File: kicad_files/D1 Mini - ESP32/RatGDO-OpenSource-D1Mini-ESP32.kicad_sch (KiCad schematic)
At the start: 7 parts, among them J1 Screw_Terminal_01x03, Q1 2N7002, Q2 AO3400A, U2 mini_esp32

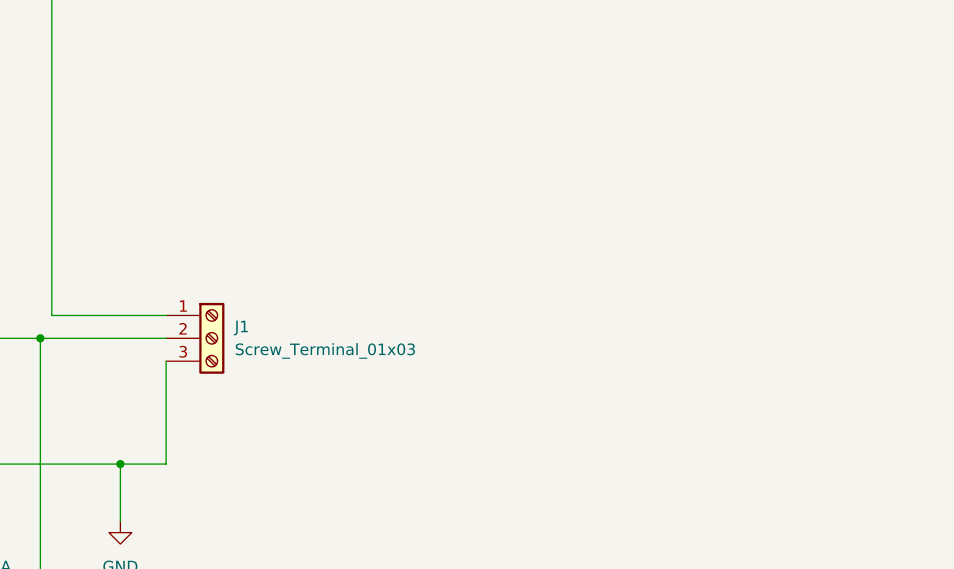
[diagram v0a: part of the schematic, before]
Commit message: Fixed Bad PCB Labeling
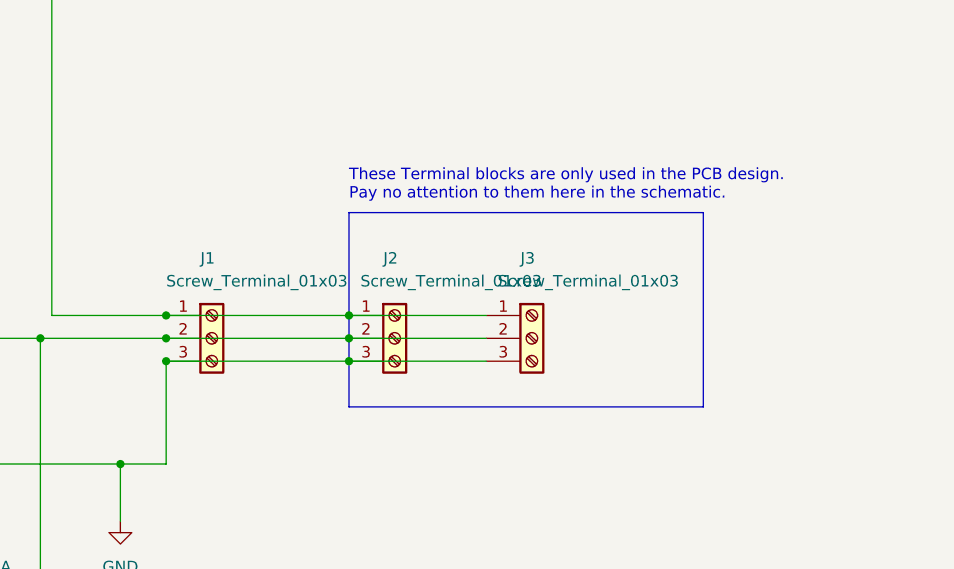
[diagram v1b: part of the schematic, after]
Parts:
- added J2: Screw_Terminal_01x03, Connector_Phoenix_MC:PhoenixContact_MCV_1,5_3-G-3.5_1x03_P3.50mm_Vertical, symbol Connector:Screw_Terminal_01x03
- added J3: Screw_Terminal_01x03, Connector_PinHeader_2.54mm:PinHeader_1x03_P2.54mm_Vertical, symbol Connector:Screw_Terminal_01x03
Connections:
- net GND: now also J2.3 (Pin_3), J3.3 (Pin_3)
- net at J1.1 (Pin_1), R1.1: now also J2.1 (Pin_1), J3.1 (Pin_1)
- net at J1.2 (Pin_2), Q1.1 (G), Q2.3 (D): now also J2.2 (Pin_2), J3.2 (Pin_2)
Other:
- note added: "These Terminal blocks are only used in the PCB design. Pay no attention to them here in the schematic."
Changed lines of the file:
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@@
 (kicad_sch (version 20230121) (generator eeschema)
   (paper "A4")
+  (junction (at 177.8 90.17) (diameter 0) (color 0 0 0 0)
+  )
   (junction (at 105.41 105.41) (diameter 0) (color 0 0 0 0)
   )
+  (junction (at 157.48 92.71) (diameter 0) (color 0 0 0 0)
+  )
   (junction (at 152.4 104.14) (diameter 0) (color 0 0 0 0)
   )
+  (junction (at 157.48 87.63) (diameter 0) (color 0 0 0 0)
+  )
+  (junction (at 177.8 92.71) (diameter 0) (color 0 0 0 0)
+  )
+  (junction (at 177.8 87.63) (diameter 0) (color 0 0 0 0)
+  )
   (junction (at 105.41 69.85) (diameter 0) (color 0 0 0 0)
   )
   (junction (at 105.41 52.07) (diameter 0) (color 0 0 0 0)
   )
+  (junction (at 157.48 90.17) (diameter 0) (color 0 0 0 0)
+  )
   (junction (at 128.27 105.41) (diameter 0) (color 0 0 0 0)
   )
@@
   (junction (at 105.41 116.84) (diameter 0) (color 0 0 0 0)
   )
+  (wire (pts (xy 177.8 92.71) (xy 193.04 92.71))
+    (stroke (width 0) (type default))
+  )
   (wire (pts (xy 52.07 118.11) (xy 105.41 118.11))
     (stroke (width 0) (type default))
@@
     (stroke (width 0) (type default))
   )
+  (wire (pts (xy 177.8 90.17) (xy 193.04 90.17))
+    (stroke (width 0) (type default))
+  )
   (wire (pts (xy 144.78 52.07) (xy 144.78 87.63))
     (stroke (width 0) (type default))
@@
     (stroke (width 0) (type default))
   )
+  (polyline (pts (xy 177.8 97.79) (xy 217.17 97.79))
+    (stroke (width 0) (type default))
+  )
   (wire (pts (xy 59.69 102.87) (xy 50.8 102.87))
     (stroke (width 0) (type default))
@@
     (stroke (width 0) (type default))
   )
+  (polyline (pts (xy 177.8 76.2) (xy 217.17 76.2))
+    (stroke (width 0) (type default))
+  )
   (wire (pts (xy 128.27 105.41) (xy 128.27 111.76))
     (stroke (width 0) (type default))
@@
     (stroke (width 0) (type default))
   )
+  (wire (pts (xy 157.48 92.71) (xy 177.8 92.71))
+    (stroke (width 0) (type default))
+  )
+  (wire (pts (xy 157.48 87.63) (xy 177.8 87.63))
+    (stroke (width 0) (type default))
+  )
   (wire (pts (xy 128.27 105.41) (xy 133.35 105.41))
     (stroke (width 0) (type default))
@@
     (stroke (width 0) (type default))
   )
+  (polyline (pts (xy 217.17 97.79) (xy 217.17 76.2))
+    (stroke (width 0) (type default))
+  )
   (wire (pts (xy 59.69 105.41) (xy 52.07 105.41))
     (stroke (width 0) (type default))
   )
+  (wire (pts (xy 157.48 90.17) (xy 177.8 90.17))
+    (stroke (width 0) (type default))
+  )
   (wire (pts (xy 120.65 116.84) (xy 105.41 116.84))
     (stroke (width 0) (type default))
@@
     (stroke (width 0) (type default))
   )
+  (wire (pts (xy 177.8 87.63) (xy 193.04 87.63))
+    (stroke (width 0) (type default))
+  )
   (wire (pts (xy 54.61 107.95) (xy 54.61 52.07))
     (stroke (width 0) (type default))
@@
     (stroke (width 0) (type default))
   )
+  (polyline (pts (xy 177.8 76.2) (xy 177.8 97.79))
+    (stroke (width 0) (type default))
+  )
   (wire (pts (xy 144.78 87.63) (xy 157.48 87.63))
     (stroke (width 0) (type default))
@@
   (wire (pts (xy 105.41 52.07) (xy 105.41 55.88))
     (stroke (width 0) (type default))
+  )
+  (text "These Terminal blocks are only used in the PCB design.\nPay no attention to them here in the schematic."
+    (at 177.8 74.93 0)
+    (effects (font (size 1.27 1.27)) (justify left bottom))
   )
   (symbol (lib_id "power:+5V") (at 92.71 54.61 90) (mirror x) (unit 1)
@@
     )
   )
+  (symbol (lib_id "Connector:Screw_Terminal_01x03") (at 182.88 90.17 0) (unit 1)
+    (in_bom yes) (on_board yes) (dnp no)
+    (property "Reference" "J2" (at 181.61 81.28 0)
+      (effects (font (size 1.27 1.27)) (justify left))
+    )
+    (property "Value" "Screw_Terminal_01x03" (at 179.07 83.82 0)
+      (effects (font (size 1.27 1.27)) (justify left))
+    )
+    (property "Footprint" "Connector_Phoenix_MC:PhoenixContact_MCV_1,5_3-G-3.5_1x03_P3.50mm_Vertical" (at 182.88 90.17 0)
+      (effects (font (size 1.27 1.27)) hide)
+    )
+    (property "Datasheet" "~" (at 182.88 90.17 0)
+      (effects (font (size 1.27 1.27)) hide)
+    )
+    (pin "1")
+    (pin "2")
+    (pin "3")
+    (instances
+      (project "RatGDO-OpenSource-D1Mini-ESP32"
+        (path "/d526daf5-1a87-4c4a-b8db-6120ccadc008"
+          (reference "J2") (unit 1)
+        )
+      )
+    )
+  )
   (symbol (lib_id "Connector:Screw_Terminal_01x03") (at 162.56 90.17 0) (unit 1)
-    (in_bom yes) (on_board yes) (dnp no) (fields_autoplaced)
-    (property "Reference" "J1" (at 165.1 88.9 0)
-      (effects (font (size 1.27 1.27)) (justify left))
-    )
-    (property "Value" "Screw_Terminal_01x03" (at 165.1 91.44 0)
+    (in_bom yes) (on_board yes) (dnp no)
+    (property "Reference" "J1" (at 161.29 81.28 0)
+      (effects (font (size 1.27 1.27)) (justify left))
+    )
+    (property "Value" "Screw_Terminal_01x03" (at 157.48 83.82 0)
       (effects (font (size 1.27 1.27)) (justify left))
     )
@@
         )
       )
+    )
+  )
+  (symbol (lib_id "Connector:Screw_Terminal_01x03") (at 198.12 90.17 0) (unit 1)
+    (in_bom yes) (on_board yes) (dnp no)
+    (property "Reference" "J3" (at 196.85 81.28 0)
+      (effects (font (size 1.27 1.27)) (justify left))
+    )
+    (property "Value" "Screw_Terminal_01x03" (at 194.31 83.82 0)
+      (effects (font (size 1.27 1.27)) (justify left))
+    )
+    (property "Footprint" "Connector_PinHeader_2.54mm:PinHeader_1x03_P2.54mm_Vertical" (at 198.12 90.17 0)
+      (effects (font (size 1.27 1.27)) hide)
+    )
+    (property "Datasheet" "~" (at 198.12 90.17 0)
+      (effects (font (size 1.27 1.27)) hide)
+    )
+    (pin "1")
+    (pin "2")
+    (pin "3")
+    (instances
+      (project "RatGDO-OpenSource-D1Mini-ESP32"
+        (path "/d526daf5-1a87-4c4a-b8db-6120ccadc008"
+          (reference "J3") (unit 1)
+        )
+      )

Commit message: Change Pin Header to Pin Socket
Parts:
- J3: footprint Connector_PinHeader_2.54mm:PinHeader_1x03_P2.54mm_Vertical -> Connector_PinSocket_2.54mm:PinSocket_1x03_P2.54mm_Vertical
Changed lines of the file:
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@@
       (effects (font (size 1.27 1.27)) (justify left))
     )
-    (property "Footprint" "Connector_PinHeader_2.54mm:PinHeader_1x03_P2.54mm_Vertical" (at 198.12 90.17 0)
+    (property "Footprint" "Connector_PinSocket_2.54mm:PinSocket_1x03_P2.54mm_Vertical" (at 198.12 90.17 0)
       (effects (font (size 1.27 1.27)) hide)
     )

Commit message: Cleaning up Schematics and making PCB layout similar for D1 Boards
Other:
- moved on the sheet: Q1, Q2
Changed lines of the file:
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@@
 (kicad_sch (version 20230121) (generator eeschema)
   (paper "A4")
+  (junction (at 105.41 104.14) (diameter 0) (color 0 0 0 0)
+  )
   (junction (at 177.8 90.17) (diameter 0) (color 0 0 0 0)
   )
-  (junction (at 105.41 105.41) (diameter 0) (color 0 0 0 0)
+  (junction (at 105.41 118.11) (diameter 0) (color 0 0 0 0)
   )
   (junction (at 157.48 92.71) (diameter 0) (color 0 0 0 0)
@@
   (junction (at 105.41 69.85) (diameter 0) (color 0 0 0 0)
   )
+  (junction (at 128.27 104.14) (diameter 0) (color 0 0 0 0)
+  )
   (junction (at 105.41 52.07) (diameter 0) (color 0 0 0 0)
   )
   (junction (at 157.48 90.17) (diameter 0) (color 0 0 0 0)
   )
-  (junction (at 128.27 105.41) (diameter 0) (color 0 0 0 0)
-  )
   (junction (at 143.51 90.17) (diameter 0) (color 0 0 0 0)
   )
-  (junction (at 105.41 116.84) (diameter 0) (color 0 0 0 0)
-  )
   (wire (pts (xy 177.8 92.71) (xy 193.04 92.71))
     (stroke (width 0) (type default))
@@
     (stroke (width 0) (type default))
   )
-  (wire (pts (xy 128.27 121.92) (xy 143.51 121.92))
-    (stroke (width 0) (type default))
-  )
-  (wire (pts (xy 137.16 90.17) (xy 137.16 60.96))
-    (stroke (width 0) (type default))
-  )
-  (wire (pts (xy 133.35 60.96) (xy 137.16 60.96))
+  (wire (pts (xy 128.27 123.19) (xy 143.51 123.19))
+    (stroke (width 0) (type default))
+  )
+  (wire (pts (xy 137.16 90.17) (xy 137.16 74.93))
+    (stroke (width 0) (type default))
+  )
+  (wire (pts (xy 132.08 74.93) (xy 137.16 74.93))
+    (stroke (width 0) (type default))
+  )
+  (wire (pts (xy 105.41 104.14) (xy 105.41 105.41))
     (stroke (width 0) (type default))
   )
@@
     (stroke (width 0) (type default))
   )
-  (wire (pts (xy 143.51 90.17) (xy 143.51 121.92))
-    (stroke (width 0) (type default))
-  )
-  (wire (pts (xy 113.03 55.88) (xy 113.03 69.85))
-    (stroke (width 0) (type default))
-  )
-  (wire (pts (xy 105.41 105.41) (xy 128.27 105.41))
+  (wire (pts (xy 143.51 90.17) (xy 143.51 123.19))
+    (stroke (width 0) (type default))
+  )
+  (wire (pts (xy 128.27 104.14) (xy 128.27 113.03))
+    (stroke (width 0) (type default))
+  )
+  (wire (pts (xy 105.41 104.14) (xy 128.27 104.14))
     (stroke (width 0) (type default))
   )
@@
     (stroke (width 0) (type default))
   )
-  (wire (pts (xy 116.84 66.04) (xy 125.73 66.04))
+  (wire (pts (xy 116.84 80.01) (xy 124.46 80.01))
     (stroke (width 0) (type default))
   )
@@
     (stroke (width 0) (type default))
   )
-  (wire (pts (xy 116.84 120.65) (xy 116.84 66.04))
+  (wire (pts (xy 116.84 120.65) (xy 116.84 80.01))
     (stroke (width 0) (type default))
   )
@@
     (stroke (width 0) (type default))
   )
-  (wire (pts (xy 105.41 118.11) (xy 105.41 116.84))
-    (stroke (width 0) (type default))
-  )
   (polyline (pts (xy 177.8 76.2) (xy 217.17 76.2))
     (stroke (width 0) (type default))
   )
-  (wire (pts (xy 128.27 105.41) (xy 128.27 111.76))
-    (stroke (width 0) (type default))
-  )
-  (wire (pts (xy 125.73 55.88) (xy 113.03 55.88))
-    (stroke (width 0) (type default))
-  )
-  (wire (pts (xy 133.35 104.14) (xy 152.4 104.14))
-    (stroke (width 0) (type default))
-  )
   (wire (pts (xy 157.48 92.71) (xy 177.8 92.71))
     (stroke (width 0) (type default))
@@
     (stroke (width 0) (type default))
   )
-  (wire (pts (xy 128.27 105.41) (xy 133.35 105.41))
+  (wire (pts (xy 128.27 104.14) (xy 152.4 104.14))
     (stroke (width 0) (type default))
   )
@@
     (stroke (width 0) (type default))
   )
-  (wire (pts (xy 120.65 116.84) (xy 105.41 116.84))
+  (wire (pts (xy 120.65 118.11) (xy 105.41 118.11))
     (stroke (width 0) (type default))
   )
@@
     (stroke (width 0) (type default))
   )
-  (wire (pts (xy 92.71 105.41) (xy 105.41 105.41))
-    (stroke (width 0) (type default))
-  )
-  (wire (pts (xy 113.03 69.85) (xy 105.41 69.85))
-    (stroke (width 0) (type default))
-  )
-  (wire (pts (xy 105.41 116.84) (xy 105.41 113.03))
+  (wire (pts (xy 92.71 104.14) (xy 105.41 104.14))
+    (stroke (width 0) (type default))
+  )
+  (wire (pts (xy 105.41 69.85) (xy 124.46 69.85))
+    (stroke (width 0) (type default))
+  )
+  (wire (pts (xy 105.41 113.03) (xy 105.41 118.11))
     (stroke (width 0) (type default))
   )
@@
     (stroke (width 0) (type default))
   )
-  (wire (pts (xy 133.35 104.14) (xy 133.35 105.41))
-    (stroke (width 0) (type default))
-  )
   (wire (pts (xy 86.36 57.15) (xy 92.71 57.15))
     (stroke (width 0) (type default))
   )
-  (wire (pts (xy 92.71 59.69) (xy 92.71 105.41))
+  (wire (pts (xy 92.71 59.69) (xy 92.71 104.14))
     (stroke (width 0) (type default))
   )
@@
     (stroke (width 0) (type default))
   )
-  (wire (pts (xy 105.41 69.85) (xy 105.41 105.41))
+  (wire (pts (xy 105.41 69.85) (xy 105.41 104.14))
     (stroke (width 0) (type default))
   )
@@
     )
   )
-  (symbol (lib_id "Connector:Screw_Terminal_01x03") (at 162.56 90.17 0) (unit 1)
+  (symbol (lib_name "Screw_Terminal_01x03_1") (lib_id "Connector:Screw_Terminal_01x03") (at 162.56 90.17 0) (unit 1)
     (in_bom yes) (on_board yes) (dnp no)
     (property "Reference" "J1" (at 161.29 81.28 0)
@@
     )
   )
-  (symbol (lib_id "Transistor_FET:AO3400A") (at 125.73 116.84 0) (mirror x) (unit 1)
-    (in_bom yes) (on_board yes) (dnp no)
-    (property "Reference" "Q2" (at 132.08 118.11 0)
-      (effects (font (size 1.27 1.27)) (justify left))
-    )
-    (property "Value" "AO3400A" (at 132.08 115.57 0)
-      (effects (font (size 1.27 1.27)) (justify left))
-    )
-    (property "Footprint" "Package_TO_SOT_SMD:SOT-23" (at 130.81 114.935 0)
+  (symbol (lib_id "Transistor_FET:AO3400A") (at 125.73 118.11 0) (mirror x) (unit 1)
+    (in_bom yes) (on_board yes) (dnp no)
+    (property "Reference" "Q2" (at 132.08 119.38 0)
+      (effects (font (size 1.27 1.27)) (justify left))
+    )
+    (property "Value" "AO3400A" (at 132.08 116.84 0)
+      (effects (font (size 1.27 1.27)) (justify left))
+    )
+    (property "Footprint" "Package_TO_SOT_SMD:SOT-23" (at 130.81 116.205 0)
       (effects (font (size 1.27 1.27) italic) (justify left) hide)
     )
-    (property "Datasheet" "http://www.aosmd.com/pdfs/datasheet/AO3400A.pdf" (at 125.73 116.84 0)
+    (property "Datasheet" "http://www.aosmd.com/pdfs/datasheet/AO3400A.pdf" (at 125.73 118.11 0)
       (effects (font (size 1.27 1.27)) (justify left) hide)
     )
@@
     )
   )
-  (symbol (lib_id "Transistor_FET:2N7002") (at 128.27 60.96 180) (unit 1)
-    (in_bom yes) (on_board yes) (dnp no)
-    (property "Reference" "Q1" (at 121.92 62.23 0)
-      (effects (font (size 1.27 1.27)) (justify left))
-    )
-    (property "Value" "2N7002" (at 121.92 59.69 0)
-      (effects (font (size 1.27 1.27)) (justify left))
-    )
-    (property "Footprint" "Package_TO_SOT_SMD:SOT-23" (at 123.19 59.055 0)
+  (symbol (lib_id "Transistor_FET:2N7002") (at 127 74.93 180) (unit 1)
+    (in_bom yes) (on_board yes) (dnp no)
+    (property "Reference" "Q1" (at 120.65 76.2 0)
+      (effects (font (size 1.27 1.27)) (justify left))
+    )
+    (property "Value" "2N7002" (at 120.65 73.66 0)
+      (effects (font (size 1.27 1.27)) (justify left))
+    )
+    (property "Footprint" "Package_TO_SOT_SMD:SOT-23" (at 121.92 73.025 0)
       (effects (font (size 1.27 1.27) italic) (justify left) hide)
     )
-    (property "Datasheet" "https://www.onsemi.com/pub/Collateral/NDS7002A-D.PDF" (at 128.27 60.96 0)
+    (property "Datasheet" "https://www.onsemi.com/pub/Collateral/NDS7002A-D.PDF" (at 127 74.93 0)
       (effects (font (size 1.27 1.27)) (justify left) hide)
     )

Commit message: Added Bare ESP8266 kicad files.
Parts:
- renumbered U2 to U1
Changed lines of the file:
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@@
   (symbol (lib_id "ESP32_mini:mini_esp32") (at 72.39 52.07 0) (unit 1)
     (in_bom yes) (on_board yes) (dnp no) (fields_autoplaced)
-    (property "Reference" "U2" (at 73.025 48.26 0)
+    (property "Reference" "U1" (at 73.025 48.26 0)
       (effects (font (size 1.27 1.27)))
     )
@@
       (project "RatGDO-OpenSource-D1Mini-ESP32"
         (path "/d526daf5-1a87-4c4a-b8db-6120ccadc008"
-          (reference "U2") (unit 1)
+          (reference "U1") (unit 1)
         )
       )
